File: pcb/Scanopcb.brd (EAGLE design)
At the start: 99.4 x 86 mm, 0 parts

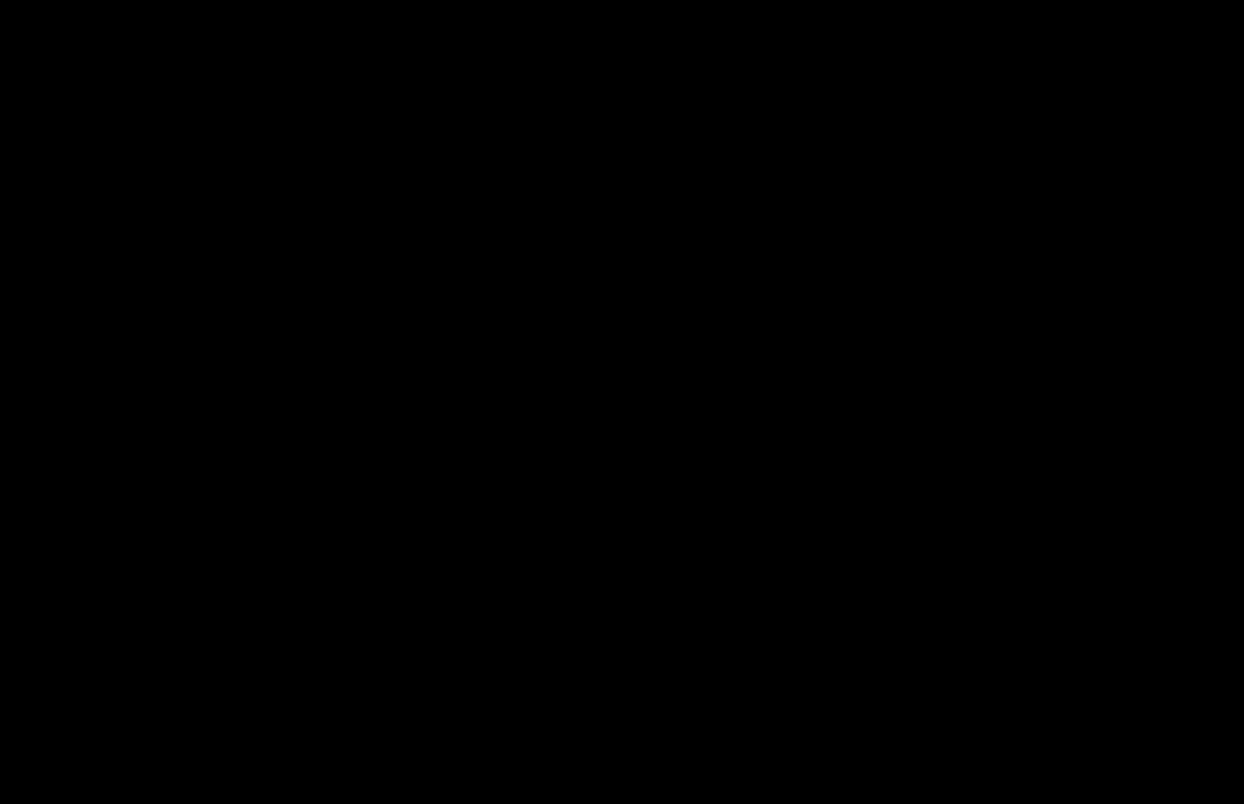
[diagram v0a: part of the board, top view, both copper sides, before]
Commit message: Added microcontroller
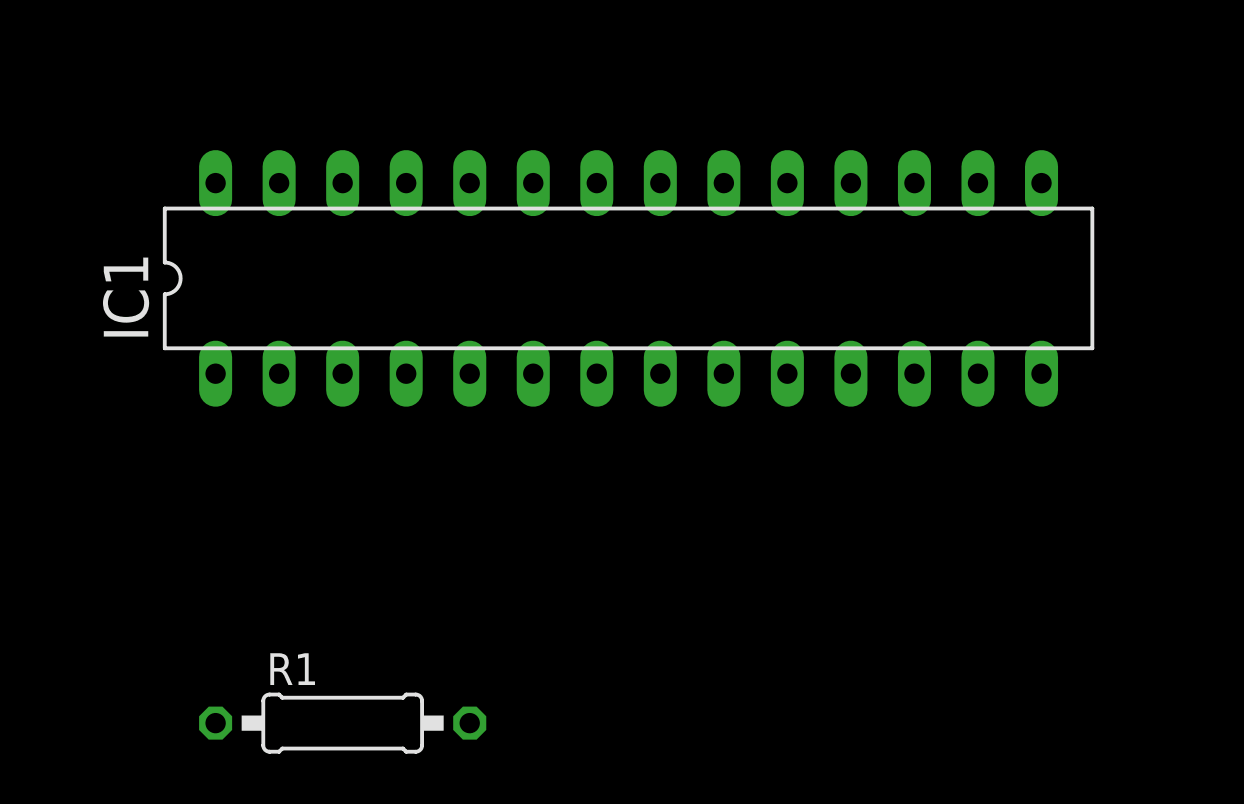
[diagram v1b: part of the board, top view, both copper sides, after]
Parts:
- added IC1: MEGA8-P, atmel:DIL28-3
- added R1: (no value), rcl:0207/10
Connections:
- new net AVCC: IC1.20
- new net GND: IC1.22, IC1.8
- new net VCC: IC1.7
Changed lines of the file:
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@@
 </autorouter>
 <elements>
+<element name="IC1" library="atmel" package="DIL28-3" value="MEGA8-P" x="24.13" y="-10.16">
+<attribute name="OC_FARNELL" value="unknown" x="24.13" y="-10.16" size="1.778" layer="27" display="off"/>
+<attribute name="OC_NEWARK" value="unknown" x="24.13" y="-10.16" size="1.778" layer="27" display="off"/>
+<attribute name="MPN" value="" x="24.13" y="-10.16" size="1.778" layer="27" display="off"/>
+<attribute name="MF" value="" x="24.13" y="-10.16" size="1.778" layer="27" display="off"/>
+</element>
+<element name="R1" library="rcl" package="0207/10" value="" x="12.7" y="-27.94"/>
 </elements>
 <signals>
+<signal name="GND">
+<contactref element="IC1" pad="8"/>
+<contactref element="IC1" pad="22"/>
+<wire x1="25.4" y1="-13.97" x2="22.86" y2="-6.35" width="0" layer="19" extent="1-1"/>
+</signal>
+<signal name="VCC">
+<contactref element="IC1" pad="7"/>
+</signal>
+<signal name="AVCC">
+<contactref element="IC1" pad="20"/>
+</signal>
 </signals>
 <errors>
